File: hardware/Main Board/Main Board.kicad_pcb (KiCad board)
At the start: 2 copper layers, 119 x 56 mm, 36 parts, among them J1 DEC Motor, J2 RA Motor, J3 Battery, J4 Joystick Debug, J5 Joystick Connector, J6 Fan, P1 Conn_02x20_Odd_Even, Q1 2N3904, Q2 2N3904, Q3 2N3904, Q4 2N3904, Q5 2N3904, Q6 S8050, U1 ELEGOO, U2 RA Driver, U3 BuckConverter, U4 BuckConverter

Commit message: Remove the Joystick Circuitry and Cleanup
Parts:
- removed J4: Joystick Debug, Connector_PinHeader_1.27mm:PinHeader_1x03_P1.27mm_Vertical
- removed J5: Joystick Connector, Connector_JST:JST_PH_B5B-PH-K_1x05_P2.00mm_Vertical
- removed Q1, Q2, Q3, Q4, Q5: 2N3904, Package_TO_SOT_THT:TO-92_Inline
- removed R1, R10, R11, R12, R3, R4, R5, R6, R8, R9: 100K, Resistor_THT:R_Axial_DIN0204_L3.6mm_D1.6mm_P1.90mm_Vertical
- removed R2, R7: 22K, Resistor_THT:R_Axial_DIN0204_L3.6mm_D1.6mm_P1.90mm_Vertical
- moved R13 37.0 mm to (223.3, 109.6), turned to 90 degrees
- moved Q6 34.5 mm to (229.7, 108.2)
- moved D1 31.0 mm to (232.7, 117.1)
- moved J6 28.8 mm to (223.9, 117.1)
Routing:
- net +5V: track 135.6 -> 35.1 mm
- net /GPIO18(GEN1)(PWM0): track 82.5 -> 10.4 mm, vias 2 -> 0
- net Net-(J4-Pad2): track 62.4 -> 0.00 mm, vias 1 -> 0
- net /GPIO10(SPI0_MOSI): track 54.8 -> 0.00 mm
- net Net-(J4-Pad3): track 36.8 -> 0.00 mm
- net /GPIO12(PWM0): track 30.7 -> 0.00 mm
- net /GPIO22(GEN3): track 26.9 -> 0.00 mm
- net Net-(J4-Pad1): track 22.9 -> 0.00 mm
- net /GPIO11(SPI0_SCK): track 13.0 -> 0.00 mm
- net /GPIO9(SPI0_MISO): track 11.3 -> 0.00 mm
- net Net-(Q3-Pad2): track 9.94 -> 0.00 mm
- net Net-(Q1-Pad2): track 7.29 -> 0.00 mm
- net Net-(Q5-Pad2): track 5.30 -> 0.00 mm
- net Net-(Q2-Pad2): track 5.09 -> 0.00 mm
- net Net-(Q4-Pad2): track 4.78 -> 0.00 mm
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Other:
- board text added: "pimount release_1.3"
- board text removed: "Joystick"
- board text removed: "pimount release_1.2"

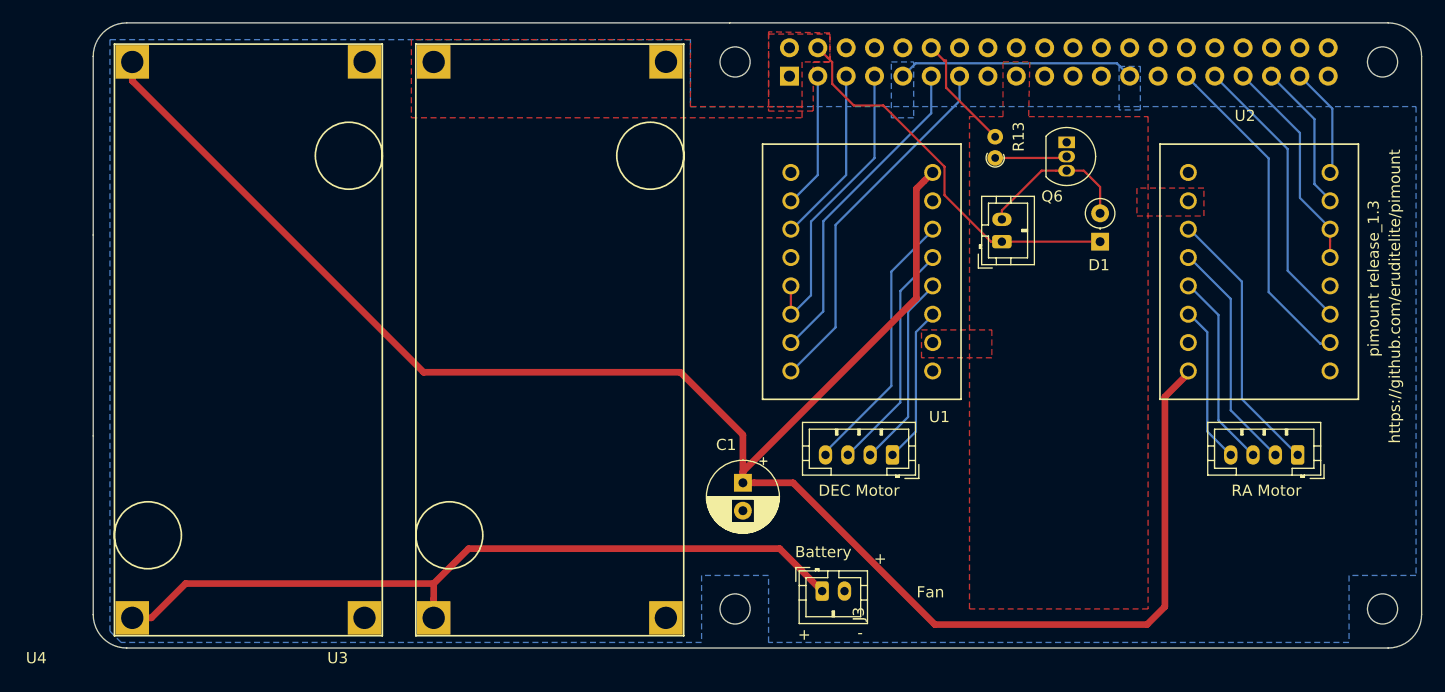
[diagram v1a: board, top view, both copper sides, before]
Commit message: Update the Schematic and Route for 2.0
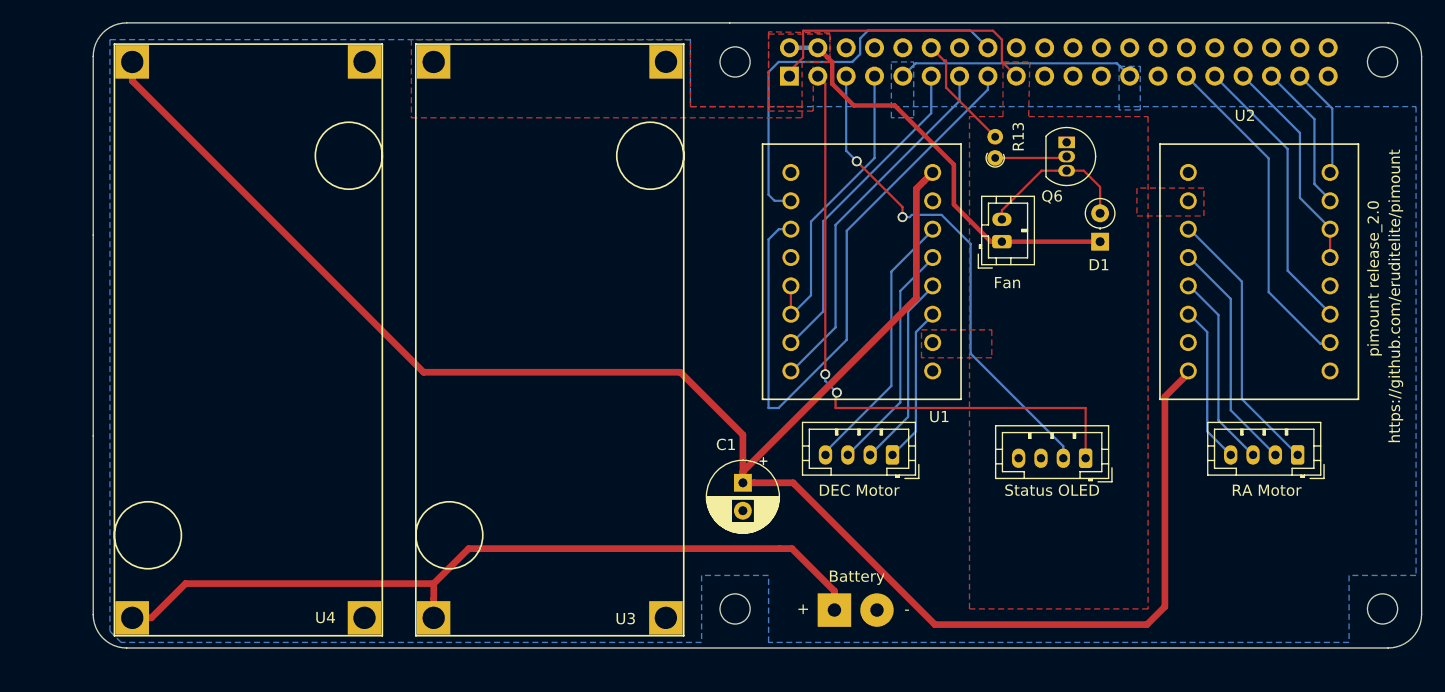
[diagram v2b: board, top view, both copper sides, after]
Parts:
- added Status OLED: OLED Display, Connector_JST:JST_PH_B4B-PH-K_1x04_P2.00mm_Vertical, F.Cu at (231.4, 136.5)
- J3: footprint Connector_JST:JST_PH_B2B-PH-K_1x02_P2.00mm_Vertical -> Connector_Wire:SolderWirePad_1x02_P3.81mm_Drill1.2mm
- moved J3 2.02 mm to (208.9, 150.1)
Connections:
- P1 pad 1: Net-(P1-Pad1) -> +3V3
- U1 pad 2: /GPIO2(SDA1) -> /GPIO23(GEN4)
- U1 pad 3: /GPIO3(SCL1) -> /GPIO22(GEN3)
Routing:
- net /GPIO22(GEN3): track 0.00 -> 55.9 mm
- net /GPIO2(SDA1): track 12.3 -> 57.4 mm, vias 0 -> 2
- net /GPIO23(GEN4): track 0.00 -> 35.9 mm
- net /GPIO3(SCL1): track 15.9 -> 44.6 mm, vias 0 -> 2
- net +3V3: track 0.00 -> 26.5 mm
- net +5V: track 35.1 -> 38.3 mm
- net Net-(J3-Pad1): track 69.0 -> 71.8 mm
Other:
- board text added: "pimount release_2.0"
- board text removed: "pimount release_1.3"
